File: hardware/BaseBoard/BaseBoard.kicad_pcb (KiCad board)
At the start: 2 copper layers, 91.4 x 109.2 mm, 91 parts, among them J1 I2C, J1-ESP1 ESP-1-L, J1-ESP2 ESP-1-L, J1-ESP3 ESP-1-L, J1-ESP4 ESP-1-L, J1-ESP5 ESP-1-L, J1-ESP6 ESP-1-L, J1-ESP7 ESP-1-L, J1-ESP8 ESP-1-L, J2 3V3P0_7, J2-ESP1 ESP-1-R, J2-ESP2 ESP-1-R, J2-ESP3 ESP-1-R, J2-ESP4 ESP-1-R, J2-ESP5 ESP-1-R, J2-ESP6 ESP-1-R, J2-ESP7 ESP-1-R, J2-ESP8 ESP-1-R, J3-BUS1 BUS1-IN1, J3-BUS2 BUS1-IN1, J3-BUS3 BUS1-IN1, J3-BUS4 BUS1-IN1, J3-BUS5 BUS1-IN1, J3-BUS6 BUS1-IN1, J3-BUS7 BUS1-IN1, J3-BUS8 BUS1-IN1, J4-BUS1 BUS1-IN2, J4-BUS2 BUS1-IN2, J4-BUS3 BUS1-IN2, J4-BUS4 BUS1-IN2, J4-BUS5 BUS1-IN2, J4-BUS6 BUS1-IN2, J4-BUS7 BUS1-IN2, J4-BUS8 BUS1-IN2, J5-BUS1 BUS1-OUT, J5-BUS2 BUS1-OUT, J5-BUS3 BUS1-OUT, J5-BUS4 BUS1-OUT, J5-BUS5 BUS1-OUT, J5-BUS6 BUS1-OUT, J5-BUS7 BUS1-OUT, J5-BUS8 BUS1-OUT, Q1-ESP1 2N3904, Q1-ESP2 2N3904, Q1-ESP3 2N3904, Q1-ESP4 2N3904, Q1-ESP5 2N3904, Q1-ESP6 2N3904, Q1-ESP7 2N3904, Q1-ESP8 2N3904, Q2-ESP1 AO3401A, Q2-ESP2 AO3401A, Q2-ESP3 AO3401A, Q2-ESP4 AO3401A, Q2-ESP5 AO3401A, Q2-ESP6 AO3401A, Q2-ESP7 AO3401A, Q2-ESP8 AO3401A, U1 AMS1117-3.3

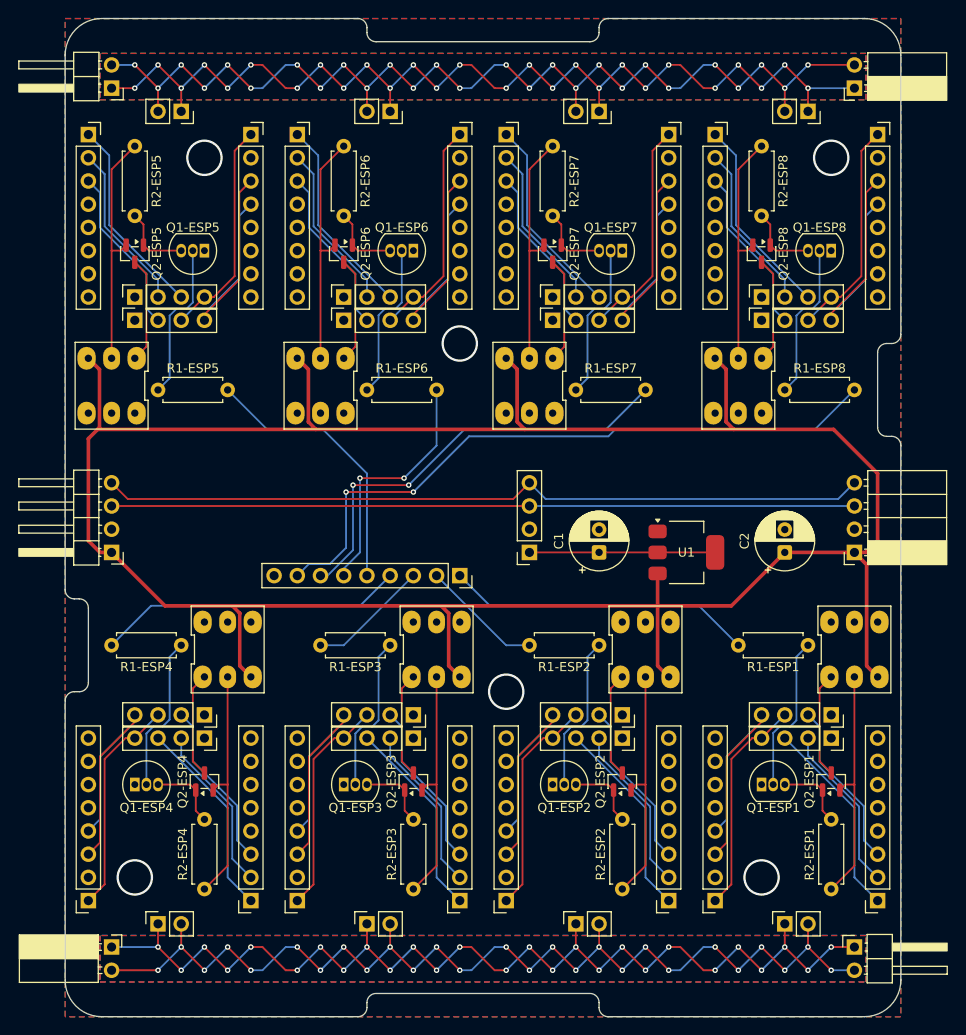
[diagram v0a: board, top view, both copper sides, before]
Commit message: Fixed wrong width of ESP modules.
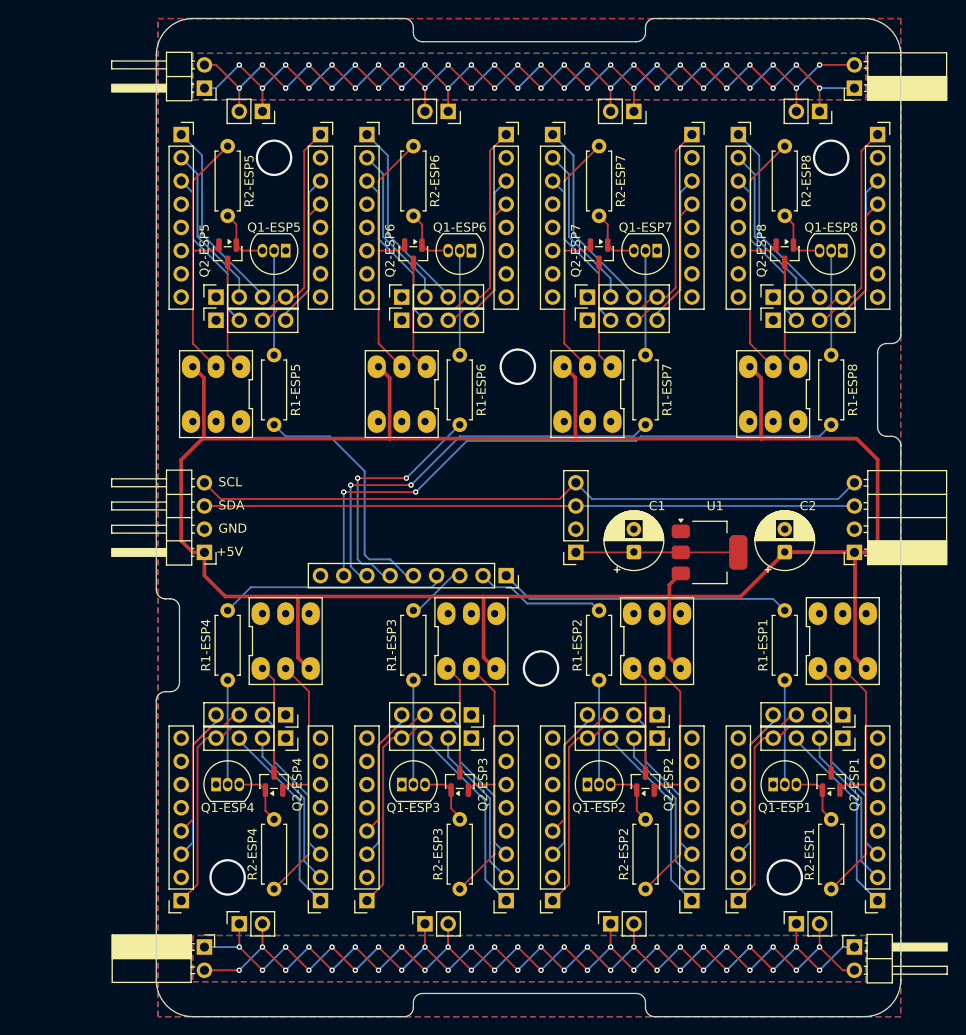
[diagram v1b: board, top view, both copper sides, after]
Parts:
- moved R1-ESP5 13.3 mm to (134.6, 54.6), turned to -90 degrees
- moved SW-ESP5 11.5 mm to (128.3, 58.9)
- moved R1-ESP6 10.9 mm to (154.9, 54.6), turned to -90 degrees
- moved BUS_IN2 10.2 mm to (127.0, 25.4)
- moved BUS_OUT1 10.2 mm to (127.0, 119.4)
- moved COM_PWR_IN1 10.2 mm to (127.0, 76.2)
- moved J1-ESP5 10.2 mm to (124.5, 30.5)
- moved J2-ESP4 10.2 mm to (124.5, 114.3)
- moved Q2-ESP5 10.2 mm to (129.5, 43.5)
- moved R2-ESP5 10.2 mm to (129.5, 31.8)
- moved SW-ESP6 8.94 mm to (148.6, 58.9)
- moved J3-BUS5 8.89 mm to (128.3, 50.8)
- moved J4-BUS5 8.89 mm to (128.3, 48.3)
- moved Q1-ESP4 8.89 mm to (128.3, 101.6)
- moved J5-BUS4 8.89 mm to (130.8, 116.8)
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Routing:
- net +5V: track 277.5 -> 253.7 mm
- net I2C_SDA: track 81.3 -> 71.1 mm
- net I2C_SCL: track 84.2 -> 74.1 mm
- net BUS2_L: track 118.8 -> 108.6 mm, vias 27 -> 26
- net BUS1_L: track 118.8 -> 108.6 mm, vias 27 -> 26
- net BUS2_H: track 118.8 -> 108.6 mm, vias 27 -> 26
- net BUS1_H: track 118.8 -> 108.6 mm, vias 27 -> 26
- net SWPIN-ESP4: track 33.6 -> 24.9 mm
- net SWPIN-ESP8: track 72.9 -> 65.5 mm
- net SWPIN-ESP3: track 13.3 -> 6.66 mm
- net Net-(Q1-ESP1-B): track 17.5 -> 11.4 mm
- net Net-(Q1-ESP6-B): track 17.5 -> 11.4 mm
- net Net-(Q1-ESP5-B): track 17.5 -> 11.4 mm
- net Net-(Q1-ESP7-B): track 17.5 -> 11.4 mm
- net Net-(Q1-ESP3-B): track 17.5 -> 11.4 mm
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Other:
- board size 91.4 x 109.2 mm -> 81.5 x 109.2 mm
- board text added: "+5V"
- board text added: "GND"
- board text added: "SCL"
- board text added: "SDA"

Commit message: Small optimizations.
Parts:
- moved J5-BUS1 1.27 mm to (191.8, 115.6)
- moved J5-BUS2 1.27 mm to (171.4, 115.6)
- moved J5-BUS3 1.27 mm to (151.1, 115.6)
- moved J5-BUS4 1.27 mm to (130.8, 115.6)
- moved BUS_IN2 1.27 mm to (127.0, 26.7)
- moved BUS_OUT2 1.27 mm to (198.1, 26.7)
- moved J5-BUS5 1.27 mm to (133.3, 29.2)
- moved J5-BUS6 1.27 mm to (153.7, 29.2)
- moved J5-BUS7 1.27 mm to (174.0, 29.2)
- moved J5-BUS8 1.27 mm to (194.3, 29.2)
- moved BUS_IN1 1.27 mm to (198.1, 118.1)
- moved BUS_OUT1 1.27 mm to (127.0, 118.1)
- moved R2-ESP1 0.76 mm to (195.6, 112.3)
- moved R2-ESP2 0.76 mm to (175.3, 112.3)
- moved R2-ESP3 0.76 mm to (154.9, 112.3)
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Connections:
- J2 pad 5: SWPIN-ESP5 -> SWPIN-ESP8
- J2 pad 6: SWPIN-ESP6 -> SWPIN-ESP7
- J2 pad 7: SWPIN-ESP7 -> SWPIN-ESP6
- J2 pad 8: SWPIN-ESP8 -> SWPIN-ESP5
- SW-ESP1 pad 6: unconnected-(SW-ESP1-Pad6) -> +5V
- SW-ESP2 pad 6: unconnected-(SW-ESP2-Pad6) -> +5V
- SW-ESP3 pad 6: unconnected-(SW-ESP3-Pad6) -> +5V
- SW-ESP4 pad 6: unconnected-(SW-ESP4-Pad6) -> +5V
- SW-ESP5 pad 6: unconnected-(SW-ESP5-Pad6) -> +5V
- SW-ESP6 pad 6: unconnected-(SW-ESP6-Pad6) -> +5V
- SW-ESP7 pad 6: unconnected-(SW-ESP7-Pad6) -> +5V
- SW-ESP8 pad 6: unconnected-(SW-ESP8-Pad6) -> +5V
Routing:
- net +5V: track 253.7 -> 307.9 mm
- net SWPIN-ESP6: track 27.0 -> 24.7 mm, vias 2 -> 0
- net SWPIN-ESP5: track 27.4 -> 25.4 mm
- net I2C_SCL: track 74.1 -> 72.6 mm
- net I2C_SDA: track 71.1 -> 72.6 mm
- net SWPIN-ESP8: track 65.5 -> 66.9 mm, vias 2 -> 0
- net Net-(Q1-ESP1-C): track 6.85 -> 5.95 mm
- net Net-(Q2-ESP8-S): track 29.9 -> 29.1 mm
- net Net-(Q2-ESP7-S): track 29.9 -> 29.1 mm
- net Net-(Q2-ESP6-S): track 29.9 -> 29.1 mm
- net Net-(Q2-ESP5-S): track 29.9 -> 29.1 mm
- net Net-(Q2-ESP4-S): track 29.9 -> 29.1 mm
- net Net-(Q2-ESP3-S): track 29.9 -> 29.1 mm
- net Net-(Q2-ESP2-S): track 29.9 -> 29.1 mm
- net Net-(Q1-ESP8-C): track 6.71 -> 5.95 mm
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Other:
- board size 81.5 x 109.2 mm -> 81.3 x 106.7 mm

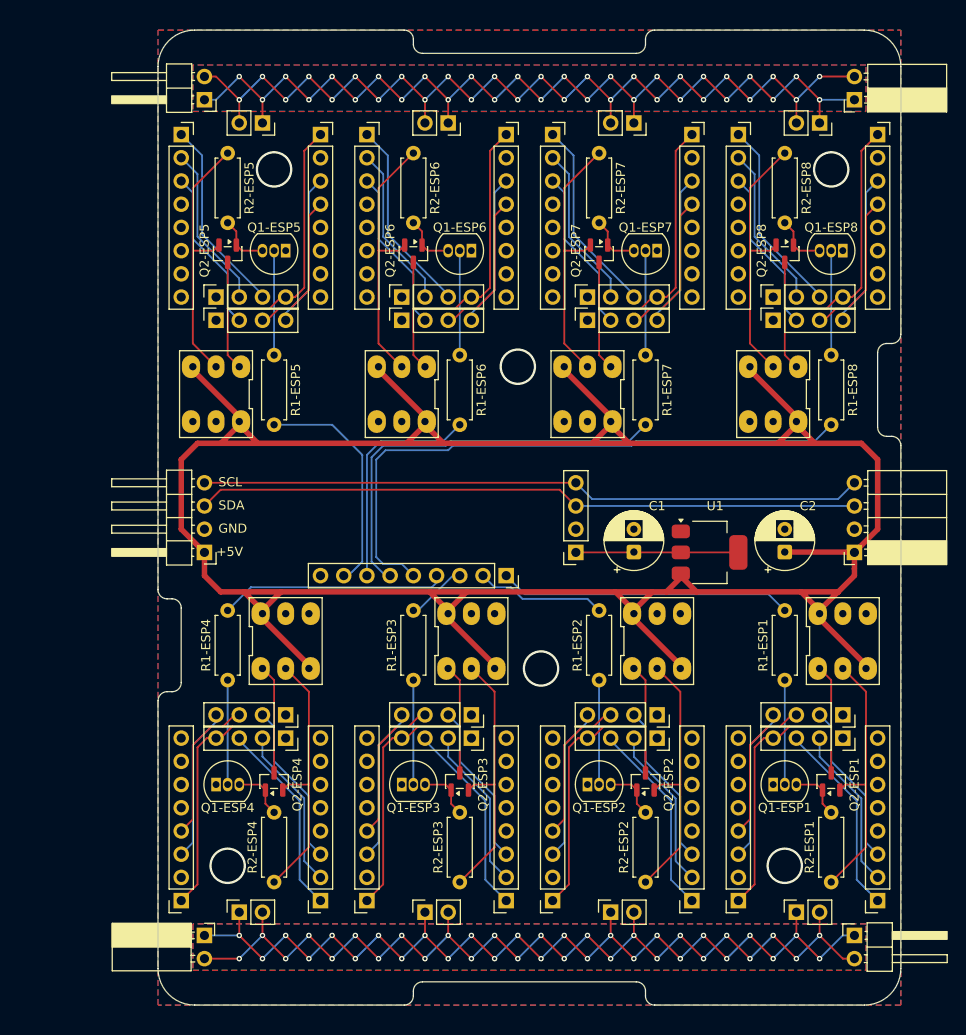
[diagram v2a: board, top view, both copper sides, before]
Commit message: Added some more labels.
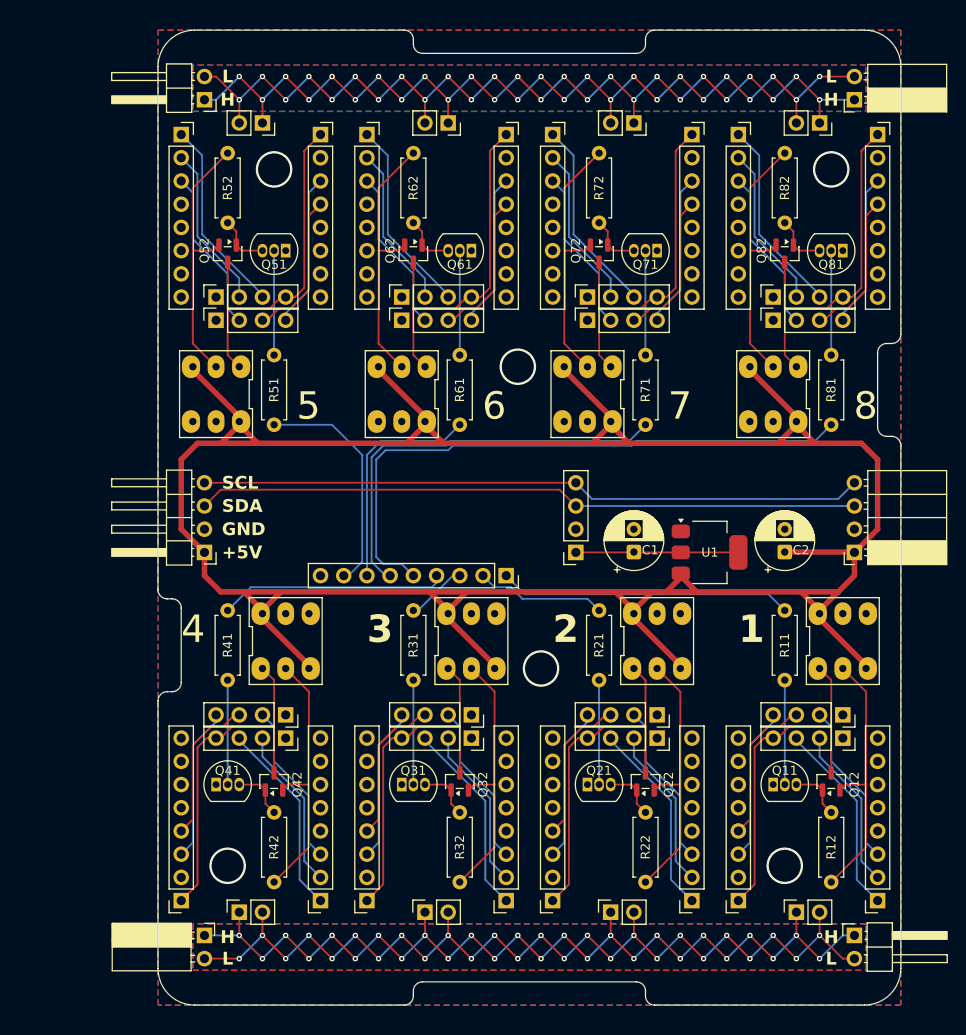
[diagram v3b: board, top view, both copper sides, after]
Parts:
- renumbered SW-ESP1 to ESP1, SW-ESP2 to ESP2, SW-ESP3 to ESP3, SW-ESP4 to ESP4, SW-ESP5 to ESP5, SW-ESP6 to ESP6, SW-ESP7 to ESP7, SW-ESP8 to ESP8, Q1-ESP1 to Q11, Q2-ESP1 to Q12, Q1-ESP2 to Q21, Q2-ESP2 to Q22, Q1-ESP3 to Q31, Q2-ESP3 to Q32, Q1-ESP4 to Q41, Q2-ESP4 to Q42, Q1-ESP5 to Q51, Q2-ESP5 to Q52, Q1-ESP6 to Q61, Q2-ESP6 to Q62, Q1-ESP7 to Q71, Q2-ESP7 to Q72, Q1-ESP8 to Q81, Q2-ESP8 to Q82, R1-ESP1 to R11, R2-ESP1 to R12, R1-ESP2 to R21, R2-ESP2 to R22, R1-ESP3 to R31, R2-ESP3 to R32, R1-ESP4 to R41, R2-ESP4 to R42, R1-ESP5 to R51, R2-ESP5 to R52, R1-ESP6 to R61, R2-ESP6 to R62, R1-ESP7 to R71, R2-ESP7 to R72, R1-ESP8 to R81, R2-ESP8 to R82
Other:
- board text added: "1"
- board text added: "2"
- board text added: "3"
- board text added: "4"
- board text added: "5"
- board text added: "6"
- board text added: "7"
- board text added: "8"
- board text added: "H"
- board text added: "L"

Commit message: Replaced two one row headers with one two row header.
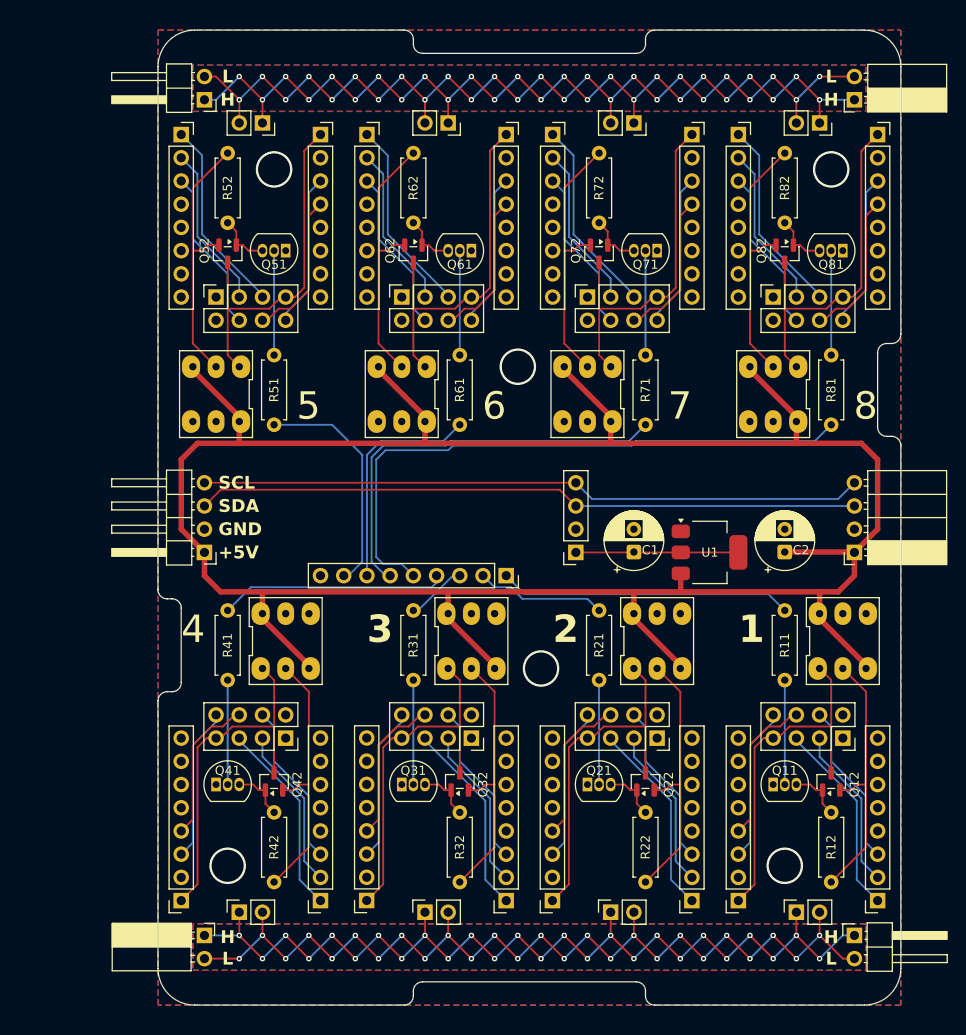
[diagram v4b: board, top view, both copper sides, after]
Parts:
- removed the J4-BUS1 at (196.8, 96.5)
- removed the J4-BUS5 at (128.3, 48.3)
- removed J5-BUS2, J5-BUS3, J5-BUS4, J5-BUS6, J5-BUS7, J5-BUS8: BUS1-OUT, Connector_PinSocket_2.54mm:PinSocket_1x02_P2.54mm_Vertical
- J3-BUS1, J3-BUS2, J3-BUS3, J3-BUS4: value BUS1-IN1 -> BUS1-IN; footprint Connector_PinSocket_2.54mm:PinSocket_1x04_P2.54mm_Vertical -> Connector_PinSocket_2.54mm:PinSocket_2x04_P2.54mm_Vertical
- J3-BUS5, J3-BUS6, J3-BUS7, J3-BUS8: value BUS1-IN1 -> BUS5-IN; footprint Connector_PinSocket_2.54mm:PinSocket_1x04_P2.54mm_Vertical -> Connector_PinSocket_2.54mm:PinSocket_2x04_P2.54mm_Vertical
- J4-BUS2, J4-BUS3, J4-BUS4, J4-BUS6, J4-BUS7, J4-BUS8: value BUS1-IN2 -> BUS1-OUT; footprint Connector_PinSocket_2.54mm:PinSocket_1x04_P2.54mm_Vertical -> Connector_PinSocket_2.54mm:PinSocket_1x02_P2.54mm_Vertical
- moved J4-BUS2 19.7 mm to (171.4, 115.6), turned to 90 degrees
- moved J4-BUS3 19.7 mm to (151.1, 115.6), turned to 90 degrees
- moved J4-BUS7 19.7 mm to (174.0, 29.2), turned to -90 degrees
- moved J4-BUS8 19.7 mm to (194.3, 29.2), turned to -90 degrees
- moved J4-BUS4 19.7 mm to (130.8, 115.6), turned to 90 degrees
- moved J4-BUS6 19.7 mm to (153.7, 29.2), turned to -90 degrees
- moved J3-BUS5 2.54 mm to (128.3, 48.3)
- moved J3-BUS6 2.54 mm to (148.6, 48.3)
- moved J3-BUS7 2.54 mm to (168.9, 48.3)
- moved J3-BUS8 2.54 mm to (189.2, 48.3)
- moved J3-BUS1 2.54 mm to (196.8, 96.5)
- moved J3-BUS2 2.54 mm to (176.5, 96.5)
- moved J3-BUS3 2.54 mm to (156.2, 96.5)
- moved J3-BUS4 2.54 mm to (135.9, 96.5)
- renumbered J5-BUS1 to J4-BUS1, J5-BUS5 to J4-BUS5
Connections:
- J3-BUS1 pad 2: Net-(J1-ESP1-Pin_3) -> GNDREF
- J3-BUS1 pad 3: Net-(J2-ESP1-Pin_4) -> Net-(J1-ESP1-Pin_2)
- J3-BUS1 pad 4: Net-(J2-ESP1-Pin_3) -> Net-(J1-ESP1-Pin_3)
- J3-BUS2 pad 2: Net-(J1-ESP2-Pin_3) -> GNDREF
- J3-BUS2 pad 3: Net-(J2-ESP2-Pin_4) -> Net-(J1-ESP2-Pin_2)
- J3-BUS2 pad 4: Net-(J2-ESP2-Pin_3) -> Net-(J1-ESP2-Pin_3)
- J3-BUS3 pad 2: Net-(J1-ESP3-Pin_3) -> GNDREF
- J3-BUS3 pad 3: Net-(J2-ESP3-Pin_4) -> Net-(J1-ESP3-Pin_2)
- J3-BUS3 pad 4: Net-(J2-ESP3-Pin_3) -> Net-(J1-ESP3-Pin_3)
- J3-BUS4 pad 2: Net-(J1-ESP4-Pin_3) -> GNDREF
- J3-BUS4 pad 3: Net-(J2-ESP4-Pin_4) -> Net-(J1-ESP4-Pin_2)
- J3-BUS4 pad 4: Net-(J2-ESP4-Pin_3) -> Net-(J1-ESP4-Pin_3)
- J3-BUS5 pad 2: Net-(J1-ESP5-Pin_3) -> GNDREF
- J3-BUS5 pad 3: Net-(J2-ESP5-Pin_4) -> Net-(J1-ESP5-Pin_2)
- J3-BUS5 pad 4: Net-(J2-ESP5-Pin_3) -> Net-(J1-ESP5-Pin_3)
- J3-BUS6 pad 2: Net-(J1-ESP6-Pin_3) -> GNDREF
- J3-BUS6 pad 3: Net-(J2-ESP6-Pin_4) -> Net-(J1-ESP6-Pin_2)
- J3-BUS6 pad 4: Net-(J2-ESP6-Pin_3) -> Net-(J1-ESP6-Pin_3)
- J3-BUS7 pad 2: Net-(J1-ESP7-Pin_3) -> GNDREF
- J3-BUS7 pad 3: Net-(J2-ESP7-Pin_4) -> Net-(J1-ESP7-Pin_2)
- J3-BUS7 pad 4: Net-(J2-ESP7-Pin_3) -> Net-(J1-ESP7-Pin_3)
- J3-BUS8 pad 2: Net-(J1-ESP8-Pin_3) -> GNDREF
- J3-BUS8 pad 3: Net-(J2-ESP8-Pin_4) -> Net-(J1-ESP8-Pin_2)
- J3-BUS8 pad 4: Net-(J2-ESP8-Pin_3) -> Net-(J1-ESP8-Pin_3)
- J4-BUS2 pad 1: GNDREF -> BUS1_H
- J4-BUS2 pad 2: Net-(J1-ESP2-Pin_2) -> BUS1_L
- J4-BUS3 pad 1: GNDREF -> BUS1_H
- J4-BUS3 pad 2: Net-(J1-ESP3-Pin_2) -> BUS1_L
- J4-BUS4 pad 1: GNDREF -> BUS1_H
- J4-BUS4 pad 2: Net-(J1-ESP4-Pin_2) -> BUS1_L
- J4-BUS6 pad 1: GNDREF -> BUS2_H
- J4-BUS6 pad 2: Net-(J1-ESP6-Pin_2) -> BUS2_L
- J4-BUS7 pad 1: GNDREF -> BUS2_H
- J4-BUS7 pad 2: Net-(J1-ESP7-Pin_2) -> BUS2_L
- J4-BUS8 pad 1: GNDREF -> BUS2_H
- J4-BUS8 pad 2: Net-(J1-ESP8-Pin_2) -> BUS2_L
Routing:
- net +5V: track 307.9 -> 271.5 mm

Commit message: Cosmetics.
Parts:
- J3-BUS1, J3-BUS2, J3-BUS3, J3-BUS4: value BUS1-IN -> BUS-IN
- J3-BUS5, J3-BUS6, J3-BUS7, J3-BUS8: value BUS5-IN -> BUS-IN
- J4-BUS1, J4-BUS2, J4-BUS3, J4-BUS4, J4-BUS5, J4-BUS6, J4-BUS7, J4-BUS8: value BUS1-OUT -> BUS-OUT
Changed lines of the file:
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@@
 			)
 		)
-		(property "Value" "BUS1-OUT"
+		(property "Value" "BUS-OUT"
 			(at 0 5.31 90)
 			(layer "F.Fab")
@@
 			)
 		)
-		(property "Value" "BUS1-IN"
+		(property "Value" "BUS-IN"
 			(at -1.27 10.39 90)
 			(layer "F.Fab")
@@
 			)
 		)
-		(property "Value" "BUS1-IN"
+		(property "Value" "BUS-IN"
 			(at -1.27 10.39 90)
 			(layer "F.Fab")
@@
 			)
 		)
-		(property "Value" "BUS5-IN"
+		(property "Value" "BUS-IN"
 			(at -1.27 10.39 90)
 			(layer "F.Fab")
@@
 			)
 		)
-		(property "Value" "BUS1-OUT"
+		(property "Value" "BUS-OUT"
 			(at 0 5.31 90)
 			(layer "F.Fab")
@@
 			)
 		)
-		(property "Value" "BUS5-IN"
+		(property "Value" "BUS-IN"
 			(at -1.27 10.39 90)
 			(layer "F.Fab")
@@
 			)
 		)
-		(property "Value" "BUS1-IN"
+		(property "Value" "BUS-IN"
 			(at -1.27 10.39 90)
 			(layer "F.Fab")
@@
 			)
 		)
-		(property "Value" "BUS1-OUT"
+		(property "Value" "BUS-OUT"
 			(at 0 5.31 90)
 			(layer "F.Fab")
@@
 			)
 		)
-		(property "Value" "BUS5-IN"
+		(property "Value" "BUS-IN"
 			(at -1.27 10.39 90)
 			(layer "F.Fab")
@@
 			)
 		)
-		(property "Value" "BUS1-OUT"
+		(property "Value" "BUS-OUT"
 			(at 0 5.31 90)
 			(layer "F.Fab")
@@
 			)
 		)
-		(property "Value" "BUS1-OUT"
+		(property "Value" "BUS-OUT"
 			(at 0 5.31 90)
 			(layer "F.Fab")
@@
 			)
 		)
-		(property "Value" "BUS1-OUT"
+		(property "Value" "BUS-OUT"
 			(at 0 5.31 90)
 			(layer "F.Fab")
@@
 			)
 		)
-		(property "Value" "BUS1-OUT"
+		(property "Value" "BUS-OUT"
 			(at 0 5.31 90)
 			(layer "F.Fab")
@@
 			)
 		)
-		(property "Value" "BUS1-OUT"
+		(property "Value" "BUS-OUT"
 			(at 0 5.31 90)
 			(layer "F.Fab")
@@
 			)
 		)
-		(property "Value" "BUS5-IN"
+		(property "Value" "BUS-IN"
 			(at -1.27 10.39 90)
 			(layer "F.Fab")
@@
 			)
 		)
-		(property "Value" "BUS1-IN"
+		(property "Value" "BUS-IN"
 			(at -1.27 10.39 90)
 			(layer "F.Fab")
